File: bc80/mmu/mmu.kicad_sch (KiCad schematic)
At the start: 9 parts, among them J1 Conn_01x06_Male, J2 Conn_01x03_Male, J3 Conn_01x03_Male, U1 74LS04, U2 74LS08, U3 74LS08, U4 74LS32, U5 74LS32, U6 74LS08

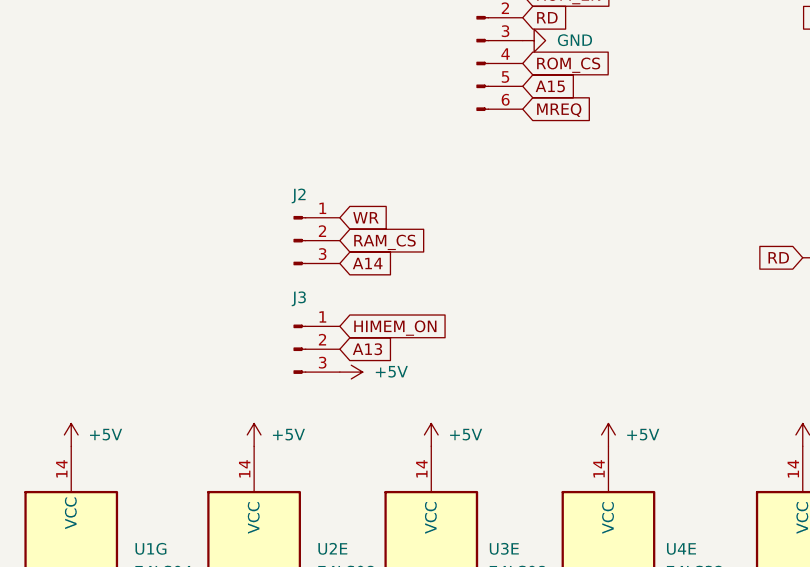
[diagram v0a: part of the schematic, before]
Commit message: a few fixes in MMU schematics and layout
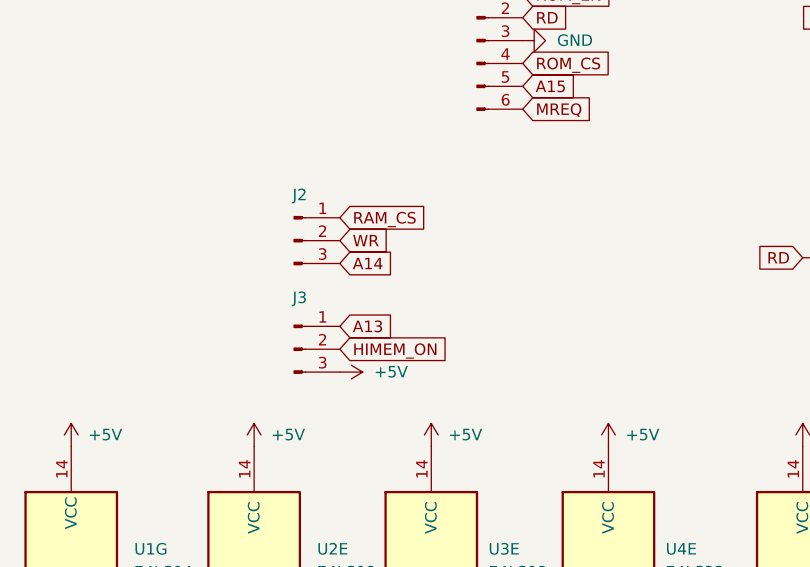
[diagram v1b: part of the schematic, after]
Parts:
- U1, U2, U3, U4, U5, U6: footprint Package_SO:SO-14_3.9x8.65mm_P1.27mm -> Package_DIP:DIP-14_W7.62mm_LongPads
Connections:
- net A13: now also J3.1 (Pin_1); no longer J3.2 (Pin_2)
- net HIMEM_ON: now also J3.2 (Pin_2); no longer J3.1 (Pin_1)
- net RAM_CS: now also J2.1 (Pin_1); no longer J2.2 (Pin_2)
- net WR: now also J2.2 (Pin_2); no longer J2.1 (Pin_1)
